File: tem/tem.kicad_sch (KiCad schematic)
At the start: 20 parts, among them J13 Conn_01x05_Pin, J14 Conn_01x02_Pin, J15 Conn_01x02_Pin, U2 MAX3051ESA+, U3 AZ1117CH-3.3TRG1

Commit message: Added TODO
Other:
- note added: "TODO: - Fuses on input, 3V3, VDD of CAN chip, MCU (and thermistor-VCC?) (should be very low current, 20mA range). Fuses should be before the decoupling caps. - Replace 100u capacitor with a lower profile one (or many ceramics in parallel). - Decide on footprints for all connectors. Also before we manufacture this: - Triple check MCU pins, CAN capabilities, ADC capabilities, SAH time, SAH charge (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"
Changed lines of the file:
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@@
     (effects (font (size 1.27 1.27)) (justify right bottom))
+  )
+  (text "TODO:\n- Fuses on input, 3V3, VDD of CAN chip, MCU (and thermistor-VCC?)\n  (should be very low current, 20mA range). Fuses should be before\n  the decoupling caps.\n- Replace 100u capacitor with a lower profile one (or many ceramics\n  in parallel).\n- Decide on footprints for all connectors.\n\nAlso before we manufacture this:\n- Triple check MCU pins, CAN capabilities, ADC capabilities, SAH time,\n  SAH charge (sampling too often could discharge the 100n capacitor on\n  each thermistor input), debugging method (current plan: PicKit3).\n- Check that we can emulate the thermistor expansion module. We would\n  need a second USB-CAN device to plug into the TEM connectors on the\n  BMS.\n- Check thermistor resistance curve (I assumed 10k at room temp)."
+    (at 28.575 168.275 0)
+    (effects (font (size 1.27 1.27)) (justify left bottom))
   )
   (text "CAN bus operating at 1MHz\n\n1.1MHz corner frequency\n\n  R = 60 || 60 = 30 ohms\n  T = RC = 141 ns\n  f = 1/(2*pi*T) = 1.13 MHz\n"

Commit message: Pull-up on reset pin
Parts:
- added R27: 10k, Resistor_SMD:R_0805_2012Metric_Pad1.20x1.40mm_HandSolder, symbol Device:R_Small
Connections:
- net +3V3: now also R27.2
- net ~{MCLR}: now also R27.1
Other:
- note added: "Current draw: 8*(3.3/10k) = 2.64mA per 8 thermistors"
- note added: "MCU current draw - less than 10mA"
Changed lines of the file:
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@@
   (junction (at 209.55 25.4) (diameter 0) (color 0 0 0 0)
+  )
+  (junction (at 111.125 131.445) (diameter 0) (color 0 0 0 0)
   )
   (junction (at 60.325 38.1) (diameter 0) (color 0 0 0 0)
@@
     (stroke (width 0) (type default))
   )
+  (wire (pts (xy 111.125 129.54) (xy 111.125 131.445))
+    (stroke (width 0) (type default))
+  )
   (wire (pts (xy 194.31 53.34) (xy 196.85 53.34))
     (stroke (width 0) (type default))
@@
     (stroke (width 0) (type default))
   )
+  (wire (pts (xy 111.125 120.65) (xy 111.125 124.46))
+    (stroke (width 0) (type default))
+  )
   (wire (pts (xy 172.72 142.24) (xy 177.8 142.24))
     (stroke (width 0) (type default))
@@
     (stroke (width 0) (type default))
   )
-  (wire (pts (xy 114.3 131.445) (xy 123.19 131.445))
+  (wire (pts (xy 104.14 131.445) (xy 111.125 131.445))
     (stroke (width 0) (type default))
   )
@@
     (stroke (width 0) (type default))
   )
+  (wire (pts (xy 111.125 131.445) (xy 123.19 131.445))
+    (stroke (width 0) (type default))
+  )
   (wire (pts (xy 240.03 54.61) (xy 240.03 55.88))
     (stroke (width 0) (type default))
@@
   (wire (pts (xy 209.55 22.86) (xy 209.55 25.4))
     (stroke (width 0) (type default))
+  )
+  (text "MCU current draw - less than 10mA" (at 135.89 81.915 0)
+    (effects (font (size 1.27 1.27)) (justify left bottom))
   )
   (text "Shutdown and standby disabled\nAlways operating in normal mode"
@@
     (effects (font (size 1.27 1.27)) (justify right bottom))
   )
+  (text "Current draw: 8*(3.3/10k) = 2.64mA per 8 thermistors"
+    (at 201.93 95.885 0)
+    (effects (font (size 1.27 1.27)) (justify left bottom))
+  )
   (text "TODO:\n- Fuses on input, 3V3, VDD of CAN chip, MCU (and thermistor-VCC?)\n  (should be very low current, 20mA range). Fuses should be before\n  the decoupling caps.\n- Replace 100u capacitor with a lower profile one (or many ceramics\n  in parallel).\n- Decide on footprints for all connectors.\n\nAlso before we manufacture this:\n- Triple check MCU pins, CAN capabilities, ADC capabilities, SAH time,\n  SAH charge (sampling too often could discharge the 100n capacitor on\n  each thermistor input), debugging method (current plan: PicKit3).\n- Check that we can emulate the thermistor expansion module. We would\n  need a second USB-CAN device to plug into the TEM connectors on the\n  BMS.\n- Check thermistor resistance curve (I assumed 10k at room temp)."
     (at 28.575 168.275 0)
@@
     (effects (font (size 1.27 1.27)) (justify right bottom))
   )
-  (label "~{MCLR}" (at 114.3 131.445 180) (fields_autoplaced)
+  (label "~{MCLR}" (at 104.14 131.445 180) (fields_autoplaced)
     (effects (font (size 1.27 1.27)) (justify right bottom))
   )
@@
     )
   )
+  (symbol (lib_id "Device:R_Small") (at 111.125 127 180) (unit 1)
+    (in_bom yes) (on_board yes) (dnp no)
+    (property "Reference" "R27" (at 112.395 126.365 0)
+      (effects (font (size 1.27 1.27)) (justify right))
+    )
+    (property "Value" "10k" (at 112.395 128.27 0)
+      (effects (font (size 1.27 1.27)) (justify right))
+    )
+    (property "Footprint" "Resistor_SMD:R_0805_2012Metric_Pad1.20x1.40mm_HandSolder" (at 111.125 127 0)
+      (effects (font (size 1.27 1.27)) hide)
+    )
+    (property "Datasheet" "https://www.mouser.co.uk/datasheet/2/427/dcrcwife3-1761849.pdf" (at 111.125 127 0)
+      (effects (font (size 1.27 1.27)) hide)
+    )
+    (property "Optional" "True" (at 111.125 127 0)
+      (effects (font (size 1.27 1.27)) hide)
+    )
+    (property "Order Code" "" (at 111.125 127 0)
+      (effects (font (size 1.27 1.27)) hide)
+    )
+    (property "Supplier" "Mouser" (at 111.125 127 0)
+      (effects (font (size 1.27 1.27)) hide)
+    )
+    (pin "1")
+    (pin "2")
+    (instances
+      (project "tem"
+        (path "/6a3afad0-3c0a-469c-ab0e-27be741b4ec6"
+          (reference "R27") (unit 1)
+        )
+      )
+      (project "vcu"
+        (path "/d2151cc9-0acc-4d18-a050-63c63ade8261/7285d321-62f2-4f5f-9ad9-4b63044720b5"
+          (reference "R16") (unit 1)
+        )
+        (path "/d2151cc9-0acc-4d18-a050-63c63ade8261/0a463a03-a21c-4ab4-b35a-61b3e0bc2af9"
+          (reference "R18") (unit 1)
+        )
+      )
+    )
+  )
   (symbol (lib_id "power:+3V3") (at 209.55 22.86 0) (unit 1)
     (in_bom yes) (on_board yes) (dnp no)
@@
         )
       )
+    )
+  )
+  (symbol (lib_id "power:+3V3") (at 111.125 120.65 0) (unit 1)
+    (in_bom yes) (on_board yes) (dnp no) (fields_autoplaced)
+    (property "Reference" "#PWR079" (at 111.125 124.46 0)
+      (effects (font (size 1.27 1.27)) hide)
+    )
+    (property "Value" "+3V3" (at 111.125 116.205 0)
+      (effects (font (size 1.27 1.27)))
+    )
+    (property "Footprint" "" (at 111.125 120.65 0)
+      (effects (font (size 1.27 1.27)) hide)
+    )
+    (property "Datasheet" "" (at 111.125 120.65 0)
+      (effects (font (size 1.27 1.27)) hide)
+    )
+    (pin "1")
+    (instances
+      (project "tem"
+        (path "/6a3afad0-3c0a-469c-ab0e-27be741b4ec6"
+          (reference "#PWR079") (unit 1)
+        )
+      )

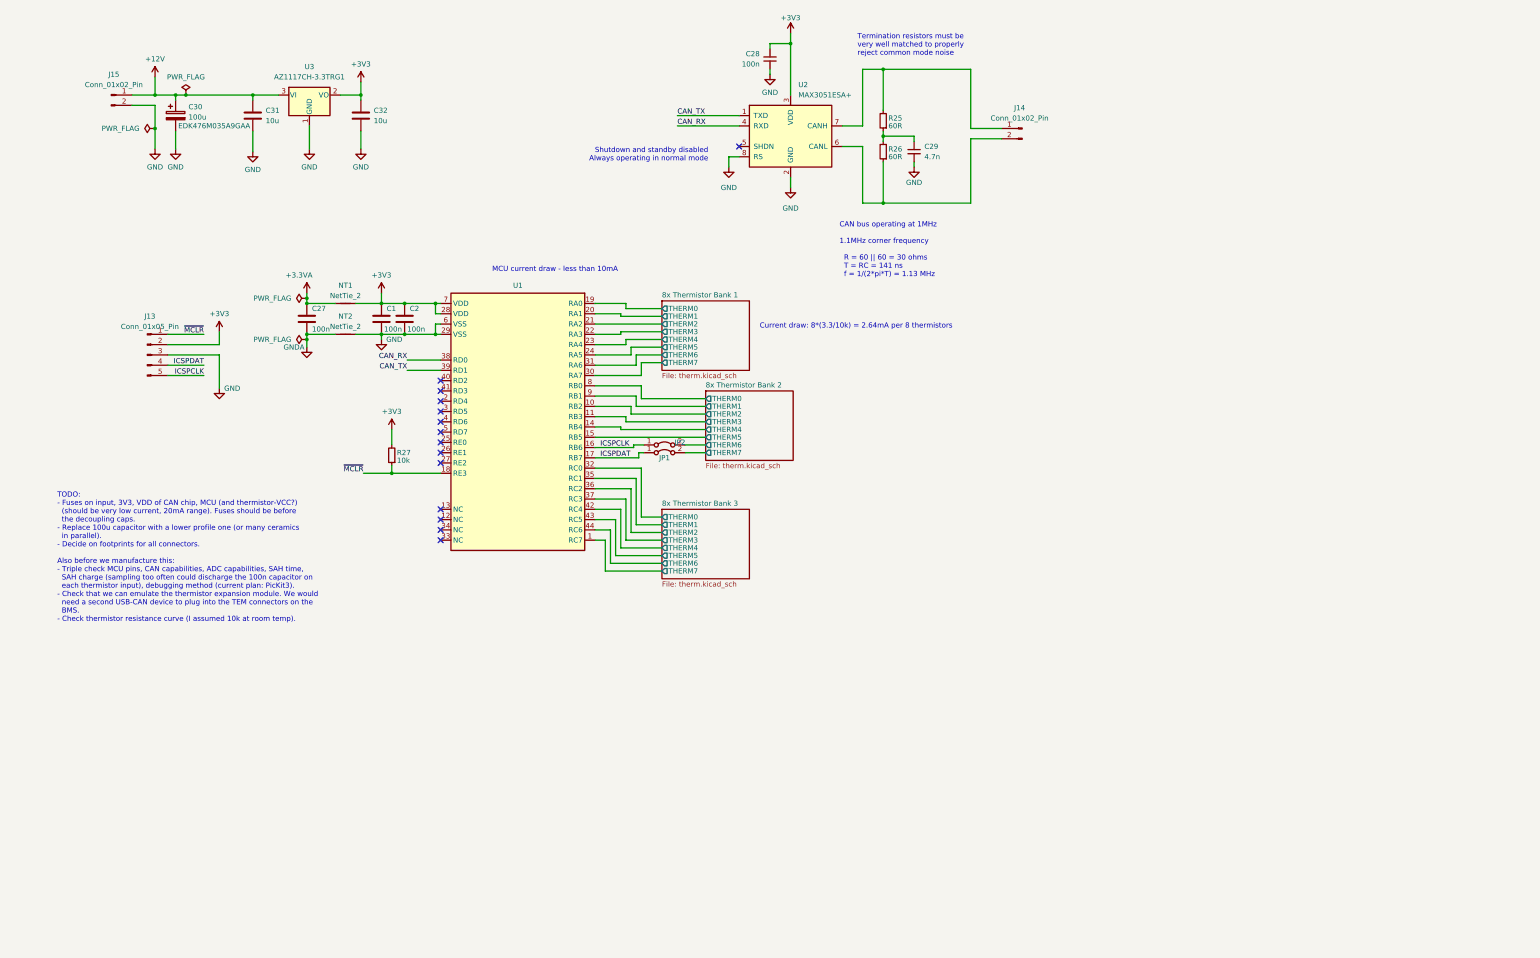
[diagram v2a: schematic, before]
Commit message: Added backup CAN chip + capacitors, changed footprints
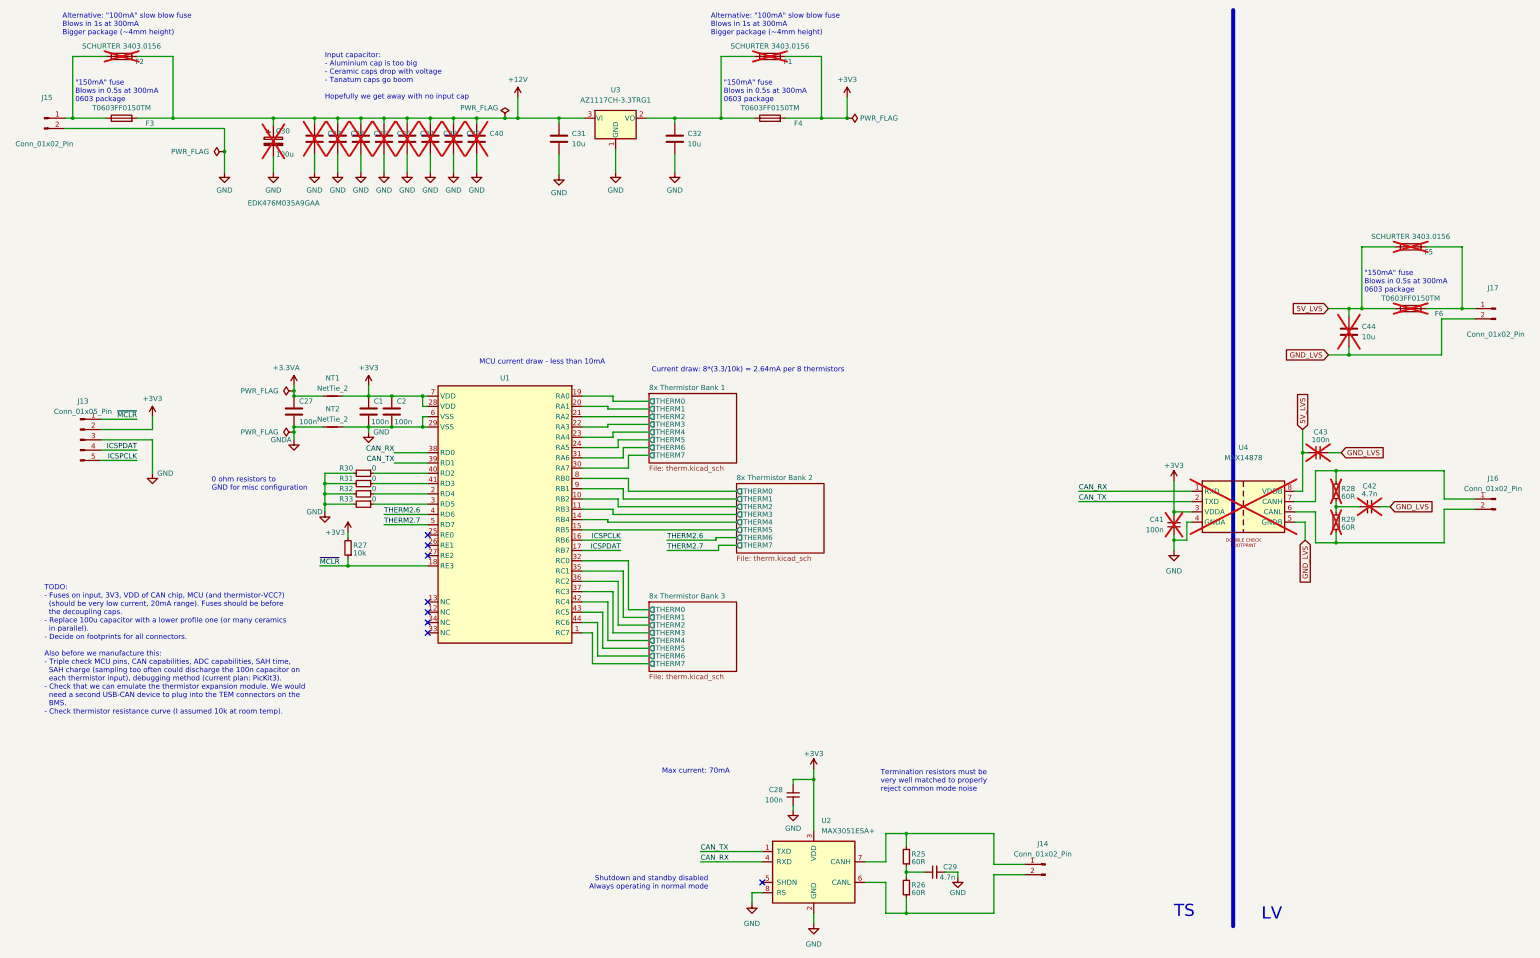
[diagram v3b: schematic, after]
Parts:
- removed JP1, JP2: Jumper_2_Bridged, Connector_PinHeader_2.54mm:PinHeader_1x02_P2.54mm_Vertical_SMD_Pin1Left, symbol Jumper:Jumper_2_Bridged
- added C33, C34, C35, C36, C37, C38, C39, C40: ~, Capacitor_SMD:C_1206_3216Metric_Pad1.33x1.80mm_HandSolder, symbol Device:C
- added C41, C43: 100n, Capacitor_SMD:C_0805_2012Metric_Pad1.18x1.45mm_HandSolder, symbol Device:C_Small
- added C42: 4.7n, Capacitor_SMD:C_0805_2012Metric_Pad1.18x1.45mm_HandSolder, symbol Device:C_Small
- added C44: 10u, Capacitor_SMD:C_0805_2012Metric_Pad1.18x1.45mm_HandSolder, symbol Device:C
- added F1, F2, F5: SCHURTER 3403.0156, Fuse:Fuse_Schurter_UMT250, symbol Device:Fuse
- added F3, F4, F6: T0603FF0150TM, Fuse:Fuse_0603_1608Metric_Pad1.05x0.95mm_HandSolder, symbol Device:Fuse
- added J16: Conn_01x02_Pin, sufst-lib:CAN_SMD, symbol Connector:Conn_01x02_Pin
- added J17: Conn_01x02_Pin, sufst-lib:Power_SMD, symbol Connector:Conn_01x02_Pin
- added R28, R29: 60R, Resistor_SMD:R_0805_2012Metric_Pad1.20x1.40mm_HandSolder, symbol Device:R_Small
- added R30, R31, R32, R33: 0, Resistor_SMD:R_0805_2012Metric_Pad1.20x1.40mm_HandSolder, symbol Device:R_Small
- added U4: MAX14878, Package_SO:SOIC-8W_5.3x5.3mm_P1.27mm, symbol SUFST:MAX14878
- C30: now not fitted
- J13: footprint Connector_PinHeader_2.54mm:PinHeader_1x05_P2.54mm_Vertical_SMD_Pin1Left -> sufst-lib:Conn5_SMD
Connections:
- net +12V: now also C33.1, C34.1, C35.1, C36.1, C37.1, C38.1, C39.1, C40.1, F2.2, F3.2; no longer J15.1 (Pin_1)
- net +3V3: now also C41.2, F1.2, F4.2, U4.3 (VDDA); no longer C32.1, U3.2 (VO)
- net CAN_RX: now also U4.1 (RXD)
- net CAN_TX: now also U4.2 (TXD)
- net GND: now also C33.2, C34.2, C35.2, C36.2, C37.2, C38.2, C39.2, C40.2, C41.1, R30.2, R31.2, R32.2, R33.2, U4.4 (GNDA)
- net at U1.2 (RD4): now also R32.1
- net at U1.3 (RD5): now also R33.1
- net THERM2.6: now reaches U1.4 (RD6)
- net at U1.40 (RD2): now also R30.1
- net at U1.41 (RD3): now also R31.1
- net THERM2.7: now reaches U1.5 (RD7)
- new net: F5.2, F6.2, J17.1 (Pin_1)
- new net: F2.1, F3.1, J15.1 (Pin_1)
- new net: C32.1, F1.1, F4.1, U3.2 (VO)
- new net: J16.1 (Pin_1), R28.2, U4.7 (CANH)
- new net: J16.2 (Pin_2), R29.1, U4.6 (CANL)
- new net: C42.1, R28.1, R29.2
- new net 5V_LVS: C43.2, C44.1, F5.1, F6.1, U4.8 (VDDB)
- new net GND_LVS: C42.2, C43.1, C44.2, J17.2 (Pin_2), U4.5 (GNDB)
- no-connect marks 14 -> 8
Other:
- note added: ""150mA" fuse Blows in 0.5s at 300mA 0603 package"
- note added: "0 ohm resistors to GND for misc configuration"
- note added: "Alternative: "100mA" slow blow fuse Blows in 1s at 300mA Bigger package (~4mm height)"
- note added: "Input capacitor: - Aluminium cap is too big - Ceramic caps drop with voltage - Tanatum caps go boom Hopefully we get away with no input cap"
- note added: "LV"
- note added: "Max current: 70mA"
- note added: "TS"
- note removed: "CAN bus operating at 1MHz 1.1MHz corner frequency R = 60 || 60 = 30 ohms T = RC = 141 ns f = 1/(2*pi*T) = 1.13 MHz"
- moved on the sheet: C1, C2, C27, C28, C29, C31, C32, J13, J14, J15, NT1, NT2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

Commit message: Layout + routing done
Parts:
- added F10, F7, F8, F9: T0603FF0250TM, Fuse:Fuse_0603_1608Metric_Pad1.05x0.95mm_HandSolder, symbol Device:Fuse
- added H1, H2, H3: MountingHole, MountingHole:MountingHole_4.3mm_M4, symbol Mechanical:MountingHole
- added R34, R35: 12, Resistor_SMD:R_0805_2012Metric_Pad1.20x1.40mm_HandSolder, symbol Device:R
- F3, F4, F6: value T0603FF0150TM -> T0603FF0250TM
- J14, J16: footprint sufst-lib:CAN_SMD -> sufst-lib:Conn2_DoubleHole
- J15, J17: footprint sufst-lib:Power_SMD -> sufst-lib:Conn2_DoubleHole
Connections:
- net +12V: now also R34.2; no longer F2.2, F3.2
- net +3V3: now also F10.2, F9.2
- net at R25.2, U2.7 (CANH): now also J14.2 (Pin_2); no longer J14.1 (Pin_1)
- net at F5.2, F6.2: now also R35.1; no longer J17.1 (Pin_1)
- net at F2.1, F3.1, J15.1 (Pin_1): now also F7.1, F8.1
- net at C32.1, F1.1, F4.1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: now also F10.1, F9.1
- net at R26.1, U2.6 (CANL): now also J14.1 (Pin_1); no longer J14.2 (Pin_2)
- new net: F2.2, F3.2, F7.2, F8.2, R34.1
- new net: J17.1 (Pin_1), R35.2
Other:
- note added: ""250mA" fuse Blows in 0.5s at 500mA 0603 package"
- note added: "Limit inrush"
- note removed: ""150mA" fuse Blows in 0.5s at 300mA 0603 package"
- moved on the sheet: J14, J17
